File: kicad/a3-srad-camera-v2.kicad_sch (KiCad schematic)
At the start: 41 parts, among them J1 BOARD_IND, J2 OUT, J3 Amphenol F32Q 1x22 P=0.5mm, SW1 PWRON, U1 AMS1117-3.3

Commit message: Add missing passives and microphone
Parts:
- added TP14: TestPoint, a3-srad-camera-v2:TestPoint_Pad_D2.0mm_Small_Courtyard, symbol Connector:TestPoint
- renumbered C8 to C6, C6 to C7, C7 to C8, J3 to J1, J1 to J2, J2 to J3, TP6 to TP10, TP13 to TP11, TP14 to TP12, TP7 to TP13, TP8 to TP15, TP15 to TP16, TP9 to TP2, TP2 to TP3, TP10 to TP4, TP3 to TP5, TP4 to TP6, TP11 to TP7, TP5 to TP8, TP12 to TP9
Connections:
- new net SOC_RECOVER: TP14.1
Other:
- sheet RV1106G2 SoC ports: added RECOVER, USB_VBUS_5V; removed USB_VBUS
- sheet USBC 2.0 OTG ports: added VBUS_DET; removed none
- moved on the sheet: C1, C2, C3, C4, C5, C6, C7, C8, FB1, H1, H2, H3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

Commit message: Footprint + silkscreen corrections
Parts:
- added TP9: TestPoint, a3-srad-camera-v2:TestPoint_Pad_D2.0mm_Small_Courtyard, symbol Connector:TestPoint
- C1, FB1, LED1, SW1, TP1, U1: now left out of the parts list
- C2: renamed from C7; footprint Capacitor_SMD:C_0805_2012Metric_Pad1.18x1.45mm_HandSolder -> Capacitor_SMD:C_1206_3216Metric; now left out of the parts list
- C3: renamed from C2; now left out of the parts list
- C4: renamed from C3; now left out of the parts list
- C5: renamed from C8; footprint Capacitor_SMD:C_0805_2012Metric_Pad1.18x1.45mm_HandSolder -> Capacitor_SMD:C_1206_3216Metric; now left out of the parts list
- C6: renamed from C4; now left out of the parts list
- C7: renamed from C5; now left out of the parts list
- C8: renamed from C6; now left out of the parts list
- J1: renamed from J3; now left out of the parts list
- J2: renamed from J1; now left out of the parts list
- J3: renamed from J2; now left out of the parts list
- R1: renamed from R3; now left out of the parts list
- R2: renamed from R4; now left out of the parts list
- R3: renamed from R1; now left out of the parts list
- R4: renamed from R2; value ? -> 120R; now left out of the parts list
- TP10: renamed from TP2; now left out of the parts list
- TP11: renamed from TP4; now left out of the parts list
- TP12: renamed from TP7; now left out of the parts list
- TP13: renamed from TP9; now left out of the parts list
- TP14: renamed from TP11; now left out of the parts list
- TP15: renamed from TP12; now left out of the parts list
- TP16: renamed from TP14; now left out of the parts list
- TP17: renamed from TP16; now left out of the parts list
- TP2: renamed from TP3; now left out of the parts list
- TP3: renamed from TP5; now left out of the parts list
- TP4: renamed from TP6; now left out of the parts list
- TP5: renamed from TP8; now left out of the parts list
- TP6: renamed from TP10; now left out of the parts list
- TP7: renamed from TP13; now left out of the parts list
- TP8: renamed from TP15; now left out of the parts list
- renumbered H3 to H2, H2 to H3
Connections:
- net VIN_5V: now also C1.1, C3.1, C4.1, C6.1, C7.2
- net VSYS_5V0: no longer C1.1, C3.1, C4.1, C6.1, C7.2
- new net EN: TP9.1
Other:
- note added: "VIN over VSYS for PMIC supply because SW1 not rated for peak PMIC current. Power consumption negligiable when rails disabled."
- moved on the sheet: TP10, TP11, TP12, TP13, TP14, TP15, TP16, TP17

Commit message: Final changes before order
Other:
- sheet STM32U575RGT6 renamed STM32U073x
- sheet TPS6521905RHBR renamed TPS65219x
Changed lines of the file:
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@@
 			(color 255 255 194 1)
 		)
-		(property "Sheetname" "TPS6521905RHBR"
+		(property "Sheetname" "TPS65219x"
 			(at 54.356 125.222 0)
 			(show_name no)
@@
 			(color 255 255 194 1)
 		)
-		(property "Sheetname" "STM32U575RGT6"
+		(property "Sheetname" "STM32U073x"
 			(at 132.08 78.232 0)
 			(show_name no)

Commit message: Minor kicad changes
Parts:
- C1, C2, C3, C4, C5, C6, C7, C8, FB1, J1, JST1, JST2, LED1, R1, R2, R4, SW1, U1: BOARD_SIDE (none) -> Front
- H1, H2, H3, H4, J2, J3, JP1, R3, TP1, TP10, TP11, TP12, TP13, TP14, TP15, TP16, TP17, TP2, TP3, TP4, TP5, TP6, TP7, TP8, TP9: now in the parts list

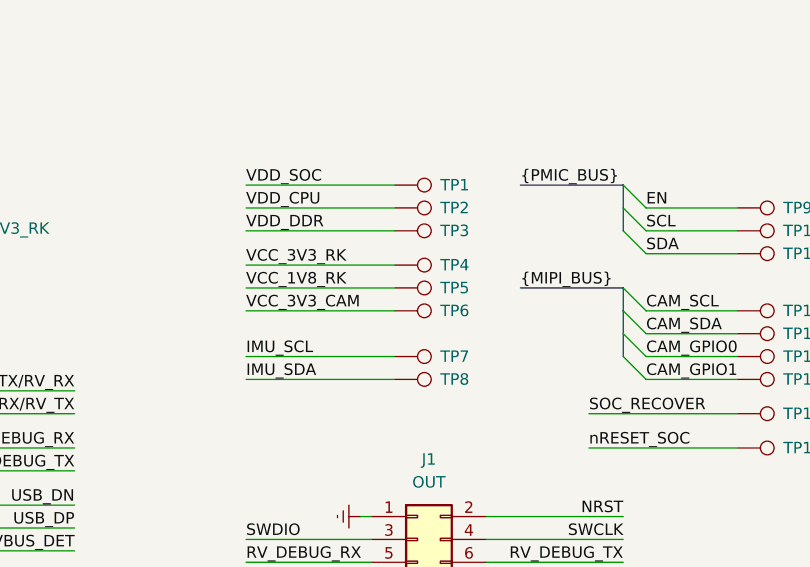
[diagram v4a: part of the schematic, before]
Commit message: Finally get PMIC working and outputting all voltages
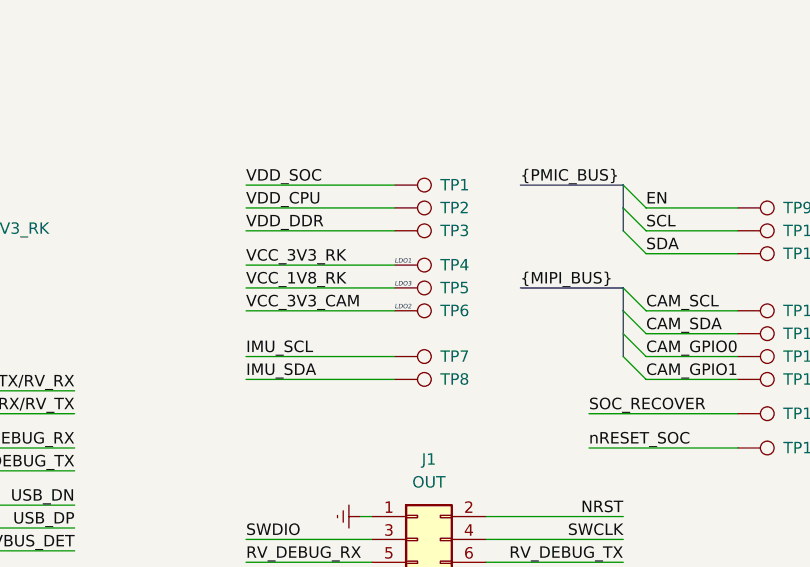
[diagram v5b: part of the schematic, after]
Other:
- note added: "LDO1"
- note added: "LDO2"
- note added: "LDO3"
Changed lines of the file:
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@@
+		)
+	)
+	(text "LDO2"
+		(exclude_from_sim no)
+		(at 198.12 124.206 0)
+		(effects
+			(font
+				(size 0.5 0.5)
+				(italic yes)
+			)
+			(justify left)
+		)
+	)
+	(text "LDO1"
+		(exclude_from_sim no)
+		(at 198.12 119.126 0)
+		(effects
+			(font
+				(size 0.5 0.5)
+				(italic yes)
+			)
+			(justify left)
 		)
 	)
@@
 		)
 	)
+	(text "LDO3"
+		(exclude_from_sim no)
+		(at 198.12 121.666 0)
+		(effects
+			(font
+				(size 0.5 0.5)
+				(italic yes)
+			)
+			(justify left)
+		)
+	)
